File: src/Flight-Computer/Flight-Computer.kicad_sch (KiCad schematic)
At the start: 39 parts, among them J1 Jumper_NO, P1 647676-2, P2 282837-2, P3 3220-20-0200-00, U1 STM32H750VBTx, U2 LMS8117AMP-3.3_NOPB, Y1 ECS-240-18-33-JGN-TR

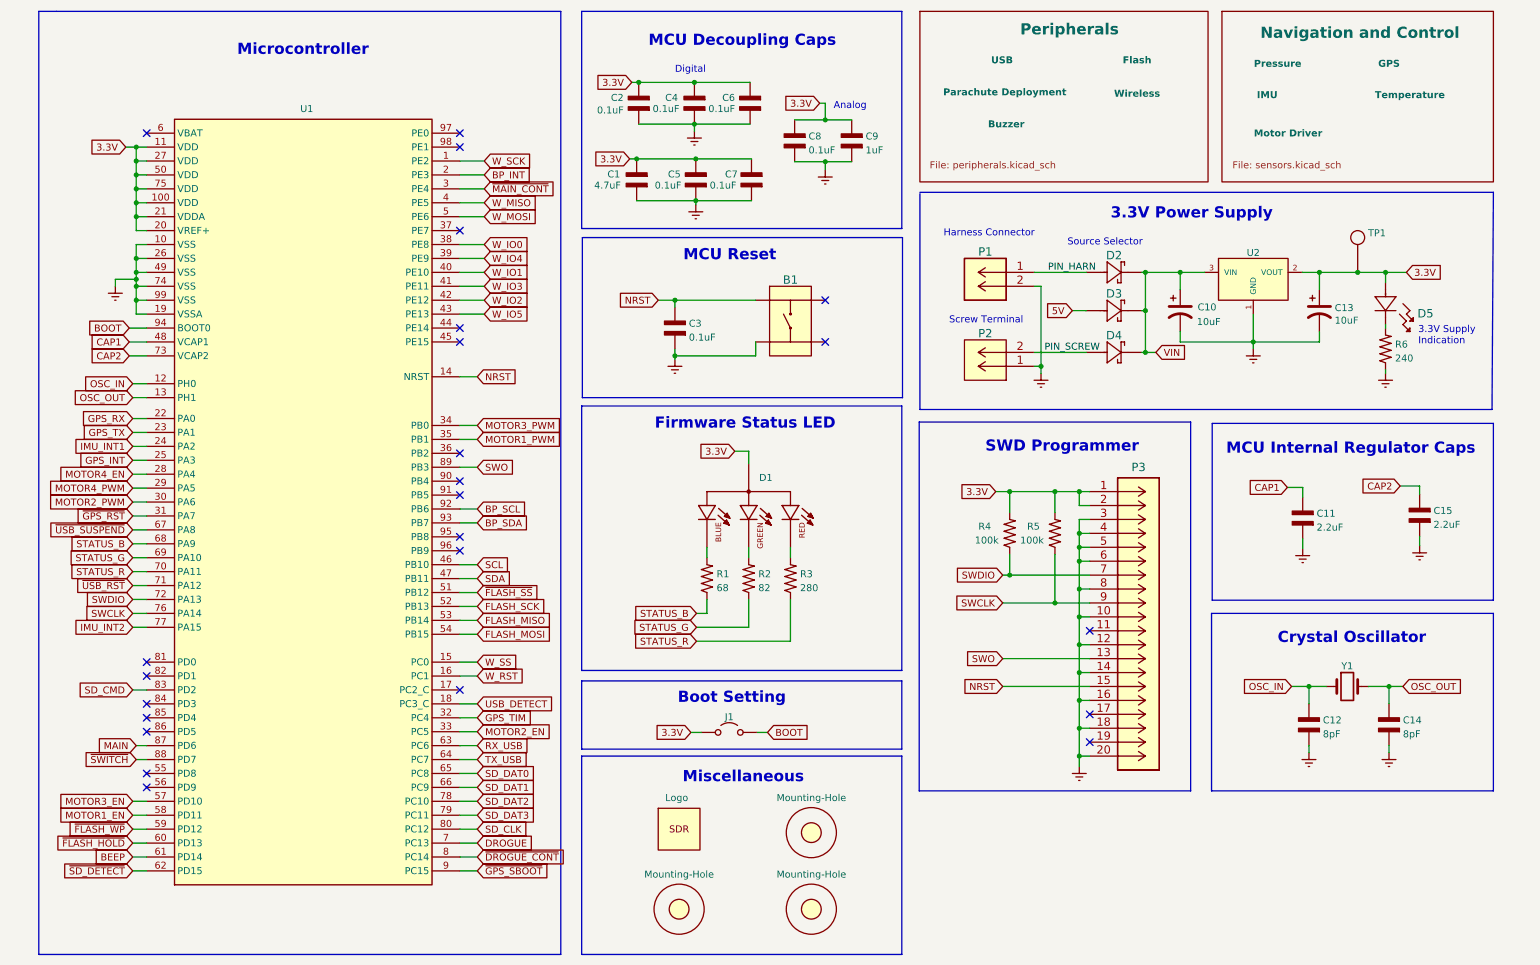
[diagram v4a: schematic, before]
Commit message: implemented magnetometer in schematic
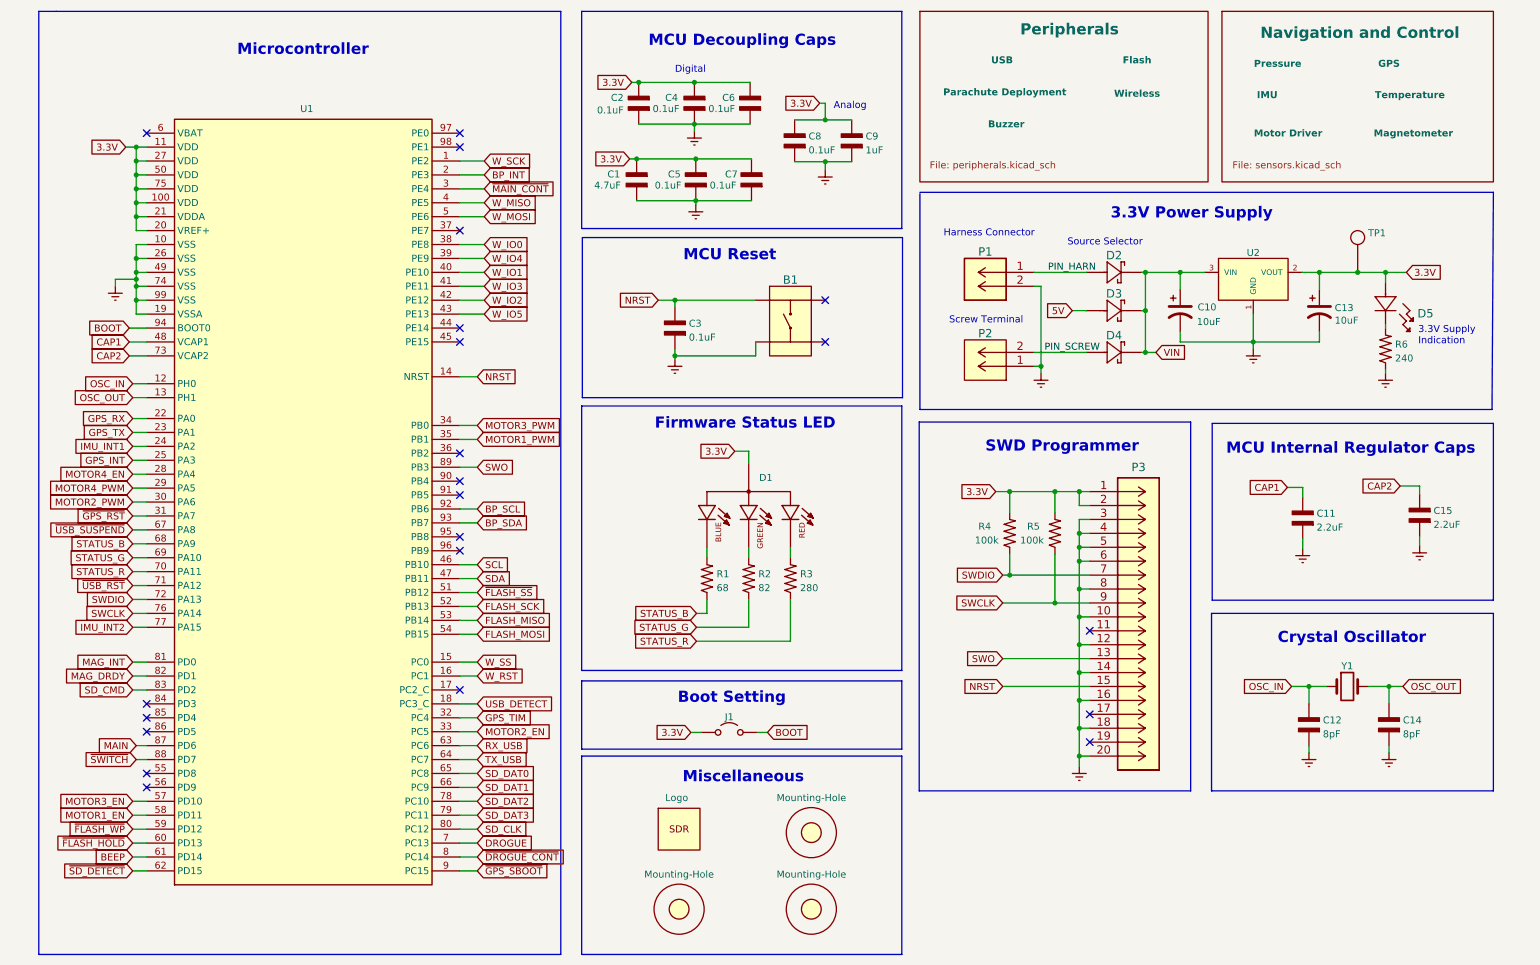
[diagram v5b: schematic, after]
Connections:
- net MAG_INT: now reaches U1.81 (PD0)
- net MAG_DRDY: now reaches U1.82 (PD1)
- no-connect marks 24 -> 22
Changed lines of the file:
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@@
   (no_connect (at 93.345 114.935))
   (no_connect (at 36.195 147.955))
-  (no_connect (at 36.195 140.335))
   (no_connect (at 36.195 150.495))
   (no_connect (at 93.345 99.695))
@@
   (no_connect (at 93.345 79.375))
   (no_connect (at 93.345 41.275))
-  (no_connect (at 36.195 137.795))
   (no_connect (at 93.345 107.315))
   (no_connect (at 36.195 145.415))
@@
     (stroke (width 0) (type default) (color 0 0 0 0))
   )
+  (wire (pts (xy 33.655 137.795) (xy 36.195 137.795))
+    (stroke (width 0) (type default) (color 0 0 0 0))
+  )
   (wire (pts (xy 146.05 99.314) (xy 146.05 101.6))
     (stroke (width 0) (type default) (color 0 0 0 0))
@@
   )
   (wire (pts (xy 93.345 64.135) (xy 97.79 64.135))
+    (stroke (width 0) (type default) (color 0 0 0 0))
+  )
+  (wire (pts (xy 33.655 140.335) (xy 36.195 140.335))
     (stroke (width 0) (type default) (color 0 0 0 0))
   )
@@
     )
   )
+  (global_label "MAG_INT" (shape input) (at 33.655 137.795 180) (fields_autoplaced)
+    (effects (font (size 1.27 1.27)) (justify right))
+    (property "Intersheet References" "${INTERSHEET_REFS}" (id 0) (at 23.6503 137.7156 0)
+      (effects (font (size 1.27 1.27)) (justify right) hide)
+    )
+  )
   (global_label "GPS_RX" (shape input) (at 33.655 93.345 180) (fields_autoplaced)
     (effects (font (size 1.27 1.27)) (justify right))
@@
     (effects (font (size 1.27 1.27)) (justify right))
     (property "Intersheet References" "${INTERSHEET_REFS}" (id 0) (at 237.1857 105.8386 0)
+      (effects (font (size 1.27 1.27)) (justify right) hide)
+    )
+  )
+  (global_label "MAG_DRDY" (shape input) (at 33.655 140.335 180) (fields_autoplaced)
+    (effects (font (size 1.27 1.27)) (justify right))
+    (property "Intersheet References" "${INTERSHEET_REFS}" (id 0) (at 21.6546 140.2556 0)
       (effects (font (size 1.27 1.27)) (justify right) hide)
     )
@@
       (effects (font (size 1.27 1.27) bold))
     )
+    (property "Field7" "Magnetometer" (id 7) (at 267.335 41.275 0)
+      (effects (font (size 1.27 1.27) bold))
+    )
   )
   (sheet (at 177.292 19.05) (size 52.578 31.115)
@@
       (reference "#PWR019") (unit 1) (value "Earth") (footprint "")
     )
+    (path "/a7215684-cee9-4aba-87f1-e5962f77da19/0a099f11-dfb5-4554-82f4-5ec16a816f5e"
+      (reference "#PWR020") (unit 1) (value "Earth") (footprint "")
+    )
+    (path "/a7215684-cee9-4aba-87f1-e5962f77da19/7b35c39c-8a9a-430a-b02f-1dcbc83d4cdf"
+      (reference "#PWR021") (unit 1) (value "Earth") (footprint "")
+    )
     (path "/a7215684-cee9-4aba-87f1-e5962f77da19/4b71cbdc-b374-4c43-a5ca-debee457df14"
       (reference "#PWR022") (unit 1) (value "Earth") (footprint "")
@@
       (reference "#PWR060") (unit 1) (value "Earth") (footprint "")
     )
+    (path "/a7215684-cee9-4aba-87f1-e5962f77da19/a119b31b-a187-497b-96f3-aa79f0d1e927"
+      (reference "#PWR061") (unit 1) (value "Earth") (footprint "")
+    )
+    (path "/a7215684-cee9-4aba-87f1-e5962f77da19/d0ea09de-337e-493a-bf5e-23a046f2e976"
+      (reference "#PWR062") (unit 1) (value "Earth") (footprint "")
+    )
     (path "/a7215684-cee9-4aba-87f1-e5962f77da19/a3048e19-c13f-4b6c-a828-4d90b1592f85"
       (reference "AE1") (unit 1) (value "0734120110") (footprint "Flight-Computer:73412-0110")
@@
       (reference "C18") (unit 1) (value "0.1uF") (footprint "Flight-Computer:CAP_0603")
     )
+    (path "/a7215684-cee9-4aba-87f1-e5962f77da19/402e3b45-316c-4666-be79-d6216fffc079"
+      (reference "C19") (unit 1) (value "0.1uF") (footprint "Flight-Computer:CAP_0603")
+    )
     (path "/a7215684-cee9-4aba-87f1-e5962f77da19/2bcd4158-516a-4eb6-9314-527fe16f509c"
       (reference "C20") (unit 1) (value "0.1uF") (footprint "Flight-Computer:CAP_0603")
@@
       (reference "C26") (unit 1) (value "1uF") (footprint "Flight-Computer:CAP_0603")
     )
+    (path "/a7215684-cee9-4aba-87f1-e5962f77da19/86adcb41-82d2-4425-bcd1-454a465affde"
+      (reference "C27") (unit 1) (value "0.1uF") (footprint "Flight-Computer:CAP_0603")
+    )
     (path "/625a26ae-4315-4158-9fbe-9e106487c8d3"
       (reference "D1") (unit 1) (value "CLMVC-FKA-CL1D1L71BB7C3C3") (footprint "Flight-Computer:CLMVC-FKA-CL1D1L71BB7C3C3")
@@
       (reference "U11") (unit 1) (value "TS391IYLT") (footprint "Flight-Computer:TS391IYLT")
     )
+    (path "/a7215684-cee9-4aba-87f1-e5962f77da19/fd13d82b-457f-4f39-a9ca-5fe07235f540"
+      (reference "U12") (unit 1) (value "BMM150") (footprint "Flight-Computer:BMM150")
+    )
     (path "/4fe127d3-8d94-46ea-90c9-64f19144e6e4"

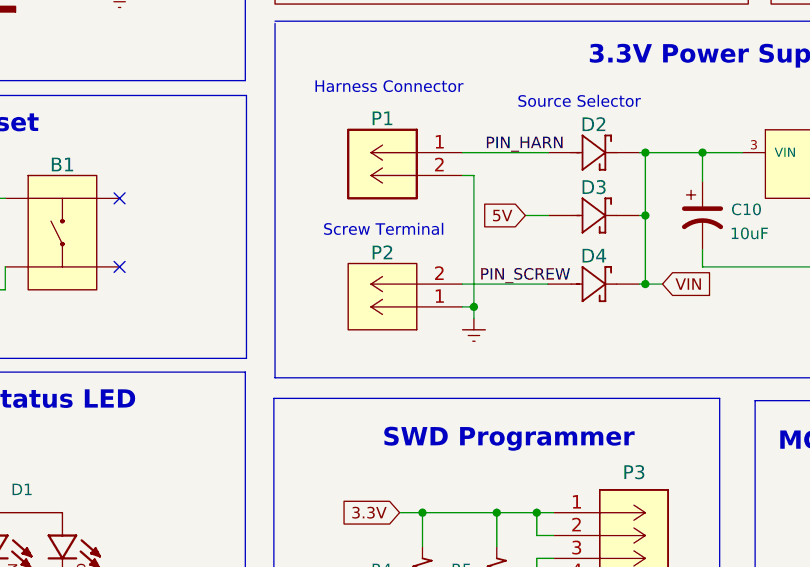
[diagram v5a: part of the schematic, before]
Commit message: replaced screw terminals with smaller parts
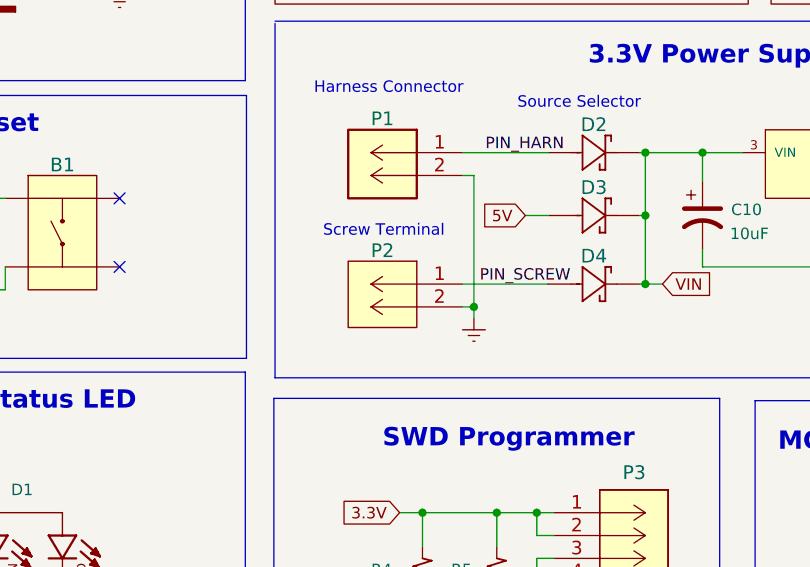
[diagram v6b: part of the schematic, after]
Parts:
- removed P2: 282837-2, Flight-Computer:282837-2, symbol Flight-Computer:282837-2
- added P2: 1546551-2, Flight-Computer:1546551-2, symbol Flight-Computer:1546551-2
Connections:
- net Earth: now also P2.2 (6)
- net PIN_SCREW: now also P2.1 (5)
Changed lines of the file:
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@@
+    (pin "2")
+  )
+  (symbol (lib_id "Flight-Computer:1546551-2") (at 198.12 81.28 0) (mirror y) (unit 1)
+    (in_bom yes) (on_board yes) (fields_autoplaced)
+    (property "Reference" "P2" (id 0) (at 189.23 77.5731 0)
+      (effects (font (size 1.524 1.524)))
+    )
+    (property "Value" "1546551-2" (id 1) (at 193.04 109.22 0)
+      (effects (font (size 1.524 1.524)) hide)
+    )
+    (property "Footprint" "Flight-Computer:1546551-2" (id 2) (at 194.31 111.76 0)
+      (effects (font (size 1.524 1.524)) hide)
+    )
+    (property "Datasheet" "" (id 3) (at 198.12 81.28 0)
+      (effects (font (size 1.524 1.524)) hide)
+    )
+    (pin "1")
     (pin "2")
   )
@@
     (property "Datasheet" "" (id 3) (at 136.144 37.084 0)
       (effects (font (size 1.27 1.27)) (justify left bottom) hide)
-    )
-    (pin "1")
-    (pin "2")
-  )
-  (symbol (lib_id "Flight-Computer:282837-2") (at 198.12 83.82 180) (unit 1)
-    (in_bom yes) (on_board yes) (fields_autoplaced)
-    (property "Reference" "P2" (id 0) (at 189.23 77.8271 0)
-      (effects (font (size 1.524 1.524)))
-    )
-    (property "Value" "282837-2" (id 1) (at 193.04 55.88 0)
-      (effects (font (size 1.524 1.524)) hide)
-    )
-    (property "Footprint" "Flight-Computer:282837-2" (id 2) (at 194.31 53.34 0)
-      (effects (font (size 1.524 1.524)) hide)
-    )
-    (property "Datasheet" "" (id 3) (at 198.12 83.82 0)
-      (effects (font (size 1.524 1.524)) hide)
     )
     (pin "1")
@@
       (reference "P1") (unit 1) (value "647676-2") (footprint "Flight-Computer:647676-2")
     )
-    (path "/8fa346f3-2124-4d55-8ce5-dad7365c6a84"
-      (reference "P2") (unit 1) (value "282837-2") (footprint "Flight-Computer:282837-2")
+    (path "/7069cbe8-cd18-407c-aad0-3f663eef6fe7"
+      (reference "P2") (unit 1) (value "1546551-2") (footprint "Flight-Computer:1546551-2")
     )
     (path "/b101f496-de41-4d70-bd94-f188bbb0c195"
@@
       (reference "P8") (unit 1) (value "USB") (footprint "Flight-Computer:10118194-0001LF")
     )
-    (path "/b65729ce-aade-4707-9cc1-eb9bb9e47e4f/08b5a367-cad3-4176-9e3c-72bdcadfa0b3"
-      (reference "P9") (unit 1) (value "282837-6") (footprint "Flight-Computer:282837-6")
-    )
-    (path "/b65729ce-aade-4707-9cc1-eb9bb9e47e4f/43748da7-f219-4f16-bf51-0c938c0af2fb"
-      (reference "P9") (unit 2) (value "282837-6") (footprint "Flight-Computer:282837-6")
-    )
-    (path "/b65729ce-aade-4707-9cc1-eb9bb9e47e4f/b7e1ac3b-4d6b-4c8f-87ee-6a99cd0f07a8"
-      (reference "P9") (unit 3) (value "282837-6") (footprint "Flight-Computer:282837-6")
+    (path "/b65729ce-aade-4707-9cc1-eb9bb9e47e4f/7647c47f-c2cb-4923-ba5b-3c428f701323"
+      (reference "P9") (unit 1) (value "1984659") (footprint "Flight-Computer:1984659")
+    )
+    (path "/b65729ce-aade-4707-9cc1-eb9bb9e47e4f/0cc0f309-354f-4a94-9fcd-19cbe68055bf"
+      (reference "P9") (unit 2) (value "1984659") (footprint "Flight-Computer:1984659")
+    )
+    (path "/b65729ce-aade-4707-9cc1-eb9bb9e47e4f/3c7f2a81-7124-4866-b422-f940f0956860"
+      (reference "P9") (unit 3) (value "1984659") (footprint "Flight-Computer:1984659")
     )
     (path "/b65729ce-aade-4707-9cc1-eb9bb9e47e4f/555fdff7-9bd3-4ee3-8c84-a02b4e5418bb"

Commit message: started rev 2 routing
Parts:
- H1, H2, H3: footprint Flight-Computer:MountingHole_4.3mm_M4_DIN965 -> Flight-Computer:MountingHole_3mm
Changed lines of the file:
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@@
     )
     (property "Value" "Mounting-Hole" (id 1) (at 133.35 176.53 0))
-    (property "Footprint" "Flight-Computer:MountingHole_4.3mm_M4_DIN965" (id 2) (at 133.35 182.88 0)
+    (property "Footprint" "Flight-Computer:MountingHole_3mm" (id 2) (at 133.35 182.88 0)
       (effects (font (size 1.27 1.27)) hide)
     )
@@
     )
     (property "Value" "Mounting-Hole" (id 1) (at 157.48 176.53 0))
-    (property "Footprint" "Flight-Computer:MountingHole_4.3mm_M4_DIN965" (id 2) (at 157.48 182.88 0)
+    (property "Footprint" "Flight-Computer:MountingHole_3mm" (id 2) (at 157.48 182.88 0)
       (effects (font (size 1.27 1.27)) hide)
     )
@@
     )
     (property "Value" "Mounting-Hole" (id 1) (at 157.48 162.56 0))
-    (property "Footprint" "Flight-Computer:MountingHole_4.3mm_M4_DIN965" (id 2) (at 157.48 168.91 0)
+    (property "Footprint" "Flight-Computer:MountingHole_3mm" (id 2) (at 157.48 168.91 0)
       (effects (font (size 1.27 1.27)) hide)
     )
@@
       (reference "#PWR060") (unit 1) (value "Earth") (footprint "")
     )
-    (path "/a7215684-cee9-4aba-87f1-e5962f77da19/a119b31b-a187-497b-96f3-aa79f0d1e927"
-      (reference "#PWR061") (unit 1) (value "Earth") (footprint "")
-    )
-    (path "/a7215684-cee9-4aba-87f1-e5962f77da19/d0ea09de-337e-493a-bf5e-23a046f2e976"
-      (reference "#PWR062") (unit 1) (value "Earth") (footprint "")
-    )
     (path "/a7215684-cee9-4aba-87f1-e5962f77da19/a3048e19-c13f-4b6c-a828-4d90b1592f85"
       (reference "AE1") (unit 1) (value "0734120110") (footprint "Flight-Computer:73412-0110")
@@
       (reference "C18") (unit 1) (value "0.1uF") (footprint "Flight-Computer:CAP_0603")
     )
-    (path "/a7215684-cee9-4aba-87f1-e5962f77da19/402e3b45-316c-4666-be79-d6216fffc079"
-      (reference "C19") (unit 1) (value "0.1uF") (footprint "Flight-Computer:CAP_0603")
-    )
     (path "/a7215684-cee9-4aba-87f1-e5962f77da19/2bcd4158-516a-4eb6-9314-527fe16f509c"
       (reference "C20") (unit 1) (value "0.1uF") (footprint "Flight-Computer:CAP_0603")
@@
       (reference "C26") (unit 1) (value "1uF") (footprint "Flight-Computer:CAP_0603")
     )
-    (path "/a7215684-cee9-4aba-87f1-e5962f77da19/86adcb41-82d2-4425-bcd1-454a465affde"
-      (reference "C27") (unit 1) (value "0.1uF") (footprint "Flight-Computer:CAP_0603")
-    )
     (path "/625a26ae-4315-4158-9fbe-9e106487c8d3"
       (reference "D1") (unit 1) (value "CLMVC-FKA-CL1D1L71BB7C3C3") (footprint "Flight-Computer:CLMVC-FKA-CL1D1L71BB7C3C3")
@@
     )
     (path "/1e520e31-7764-4bc1-9ee3-232828e917a4"
-      (reference "H1") (unit 1) (value "Mounting-Hole") (footprint "Flight-Computer:MountingHole_4.3mm_M4_DIN965")
+      (reference "H1") (unit 1) (value "Mounting-Hole") (footprint "Flight-Computer:MountingHole_3mm")
     )
     (path "/b4d39a21-7c02-4cb7-9374-fdfaaba092a9"
-      (reference "H2") (unit 1) (value "Mounting-Hole") (footprint "Flight-Computer:MountingHole_4.3mm_M4_DIN965")
+      (reference "H2") (unit 1) (value "Mounting-Hole") (footprint "Flight-Computer:MountingHole_3mm")
     )
     (path "/5c97c4bf-c343-4ea1-9d91-deda5bf47189"
-      (reference "H3") (unit 1) (value "Mounting-Hole") (footprint "Flight-Computer:MountingHole_4.3mm_M4_DIN965")
+      (reference "H3") (unit 1) (value "Mounting-Hole") (footprint "Flight-Computer:MountingHole_3mm")
     )
     (path "/bafa81bc-9c13-4533-81f7-048cec1d702b"
@@
     )
     (path "/a7215684-cee9-4aba-87f1-e5962f77da19/a00a994e-144e-4867-8953-26047cca14b2"
-      (reference "R7") (unit 1) (value "10k") (footprint "")
+      (reference "R7") (unit 1) (value "10k") (footprint "Engine-Controller:RES_0603")
     )
     (path "/a7215684-cee9-4aba-87f1-e5962f77da19/330c7051-badb-4c54-bd62-47706a91a7b3"
@@
     )
     (path "/a7215684-cee9-4aba-87f1-e5962f77da19/0f10209d-e80d-4264-9d1d-ea4f9620c93f"
-      (reference "R9") (unit 1) (value "10k") (footprint "")
+      (reference "R9") (unit 1) (value "10k") (footprint "Engine-Controller:RES_0603")
     )
     (path "/a7215684-cee9-4aba-87f1-e5962f77da19/f6d57afb-9c72-4073-9e94-a358e99f15dc"
